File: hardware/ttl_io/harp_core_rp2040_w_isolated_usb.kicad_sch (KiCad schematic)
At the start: 49 parts, among them J1 Conn_01x03_Male, J2 AudioJack3, J3 USB_C_Receptacle_USB2.0, SW1 SW_Push, U1 TPD2EUSB30, U2 ADUM4160, U3 RP2040, U4 W25Q16JVUXIQ, X1 ECS-TXO-2016

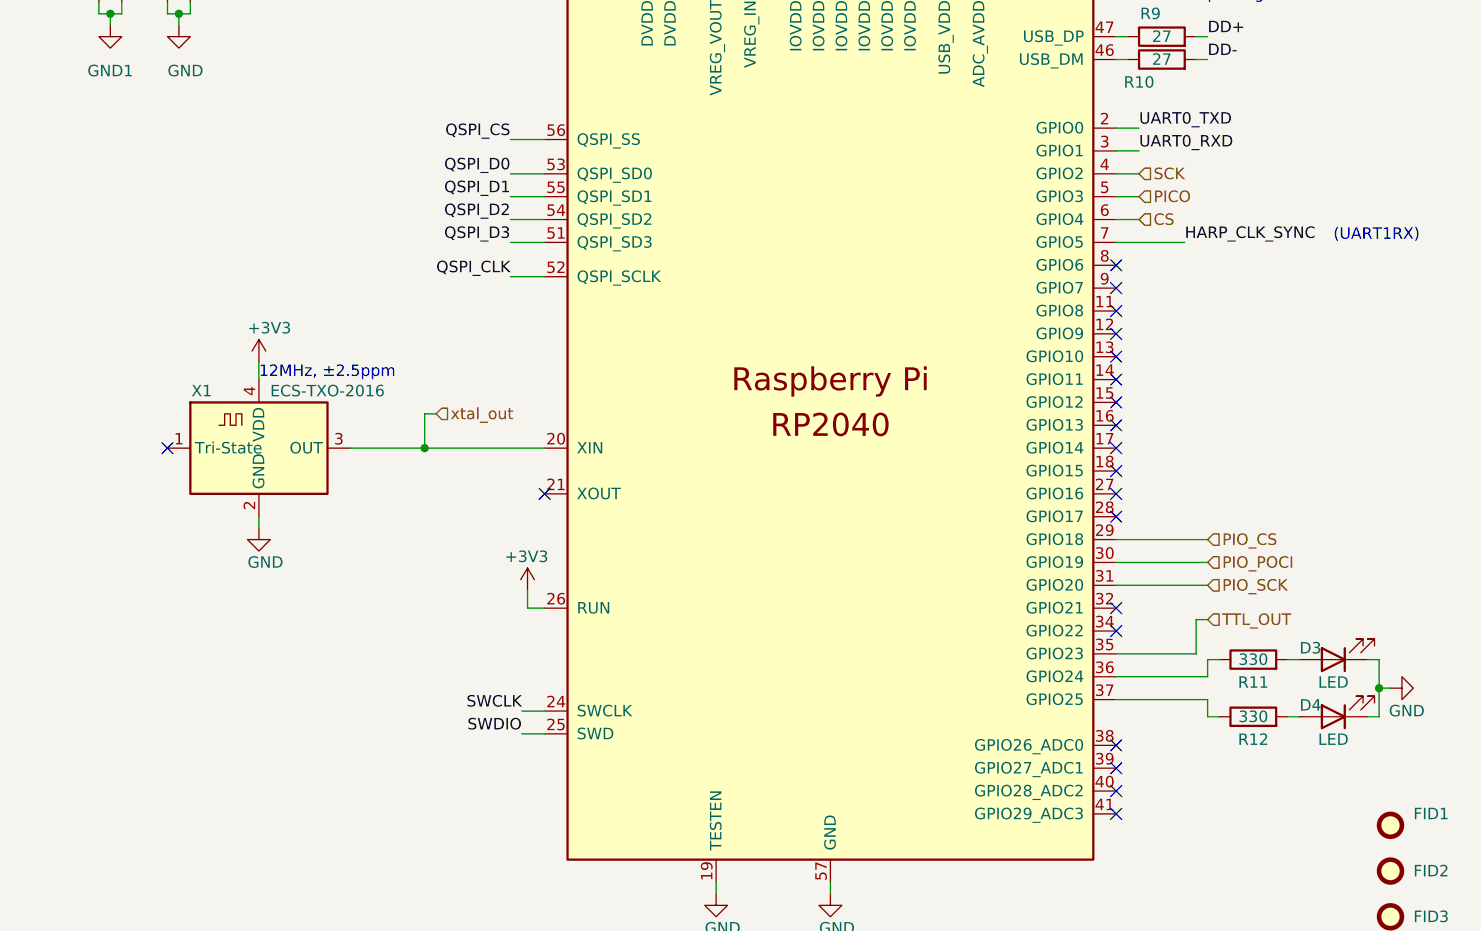
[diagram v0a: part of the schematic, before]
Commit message: draft mcu bypass with bus switches
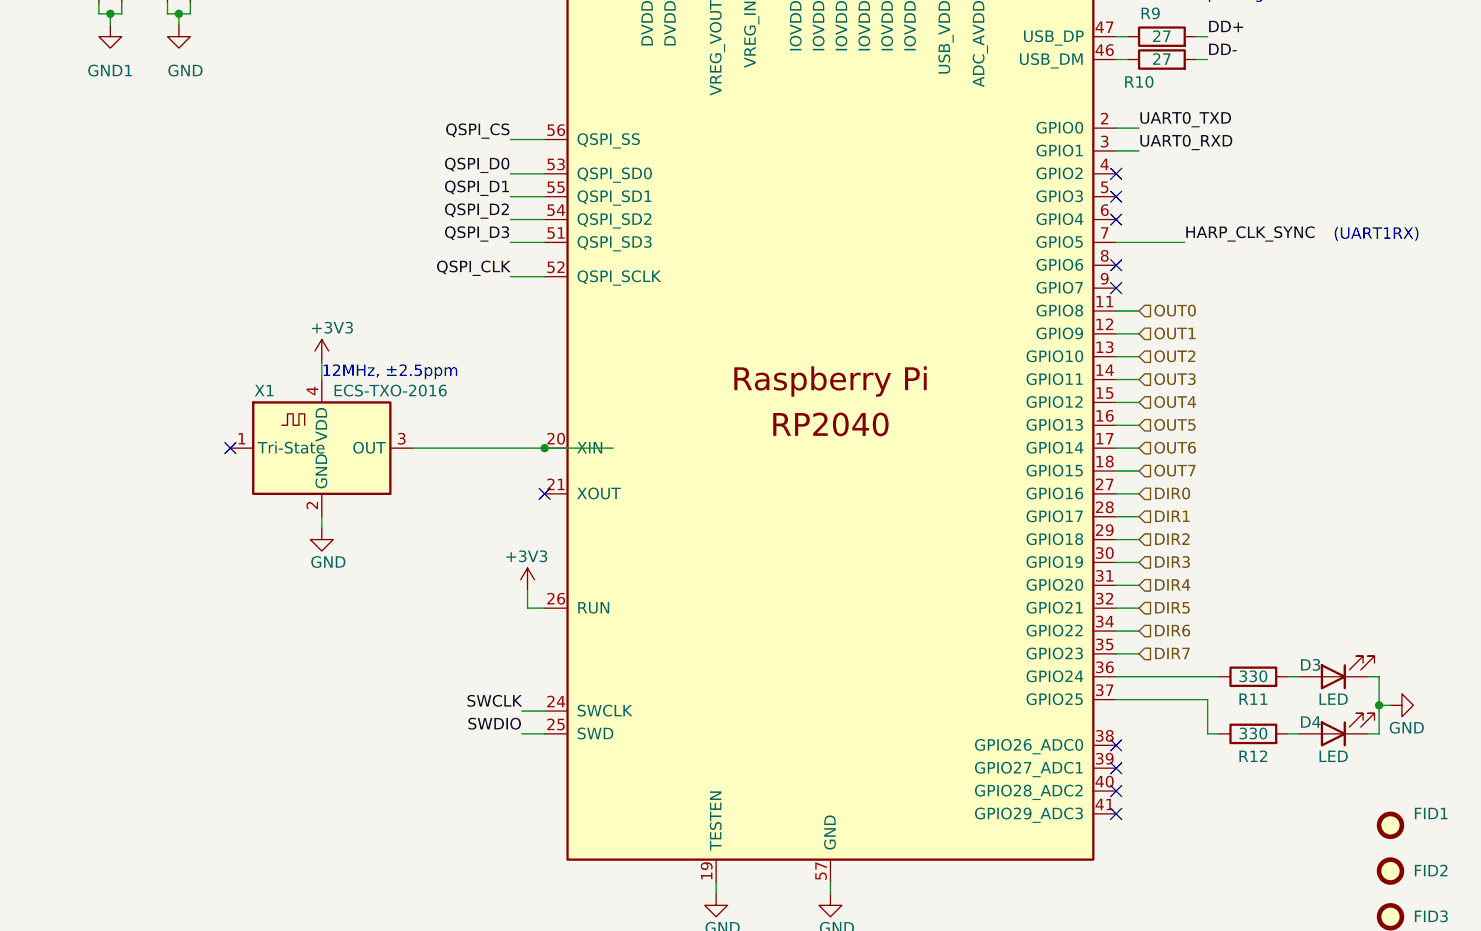
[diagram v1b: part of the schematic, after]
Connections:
- net OUT0: now reaches U3.11 (GPIO8)
- net OUT1: now reaches U3.12 (GPIO9)
- net OUT2: now reaches U3.13 (GPIO10)
- net OUT3: now reaches U3.14 (GPIO11)
- net OUT4: now reaches U3.15 (GPIO12)
- net OUT5: now reaches U3.16 (GPIO13)
- net OUT6: now reaches U3.17 (GPIO14)
- net OUT7: now reaches U3.18 (GPIO15)
- net DIR0: now reaches U3.27 (GPIO16)
- net DIR1: now reaches U3.28 (GPIO17)
- net DIR5: now reaches U3.32 (GPIO21)
- net DIR6: now reaches U3.34 (GPIO22)
- net CS: no longer names the net of U3.6 (GPIO4)
- net PICO: no longer names the net of U3.5 (GPIO3)
- net PIO_CS renamed DIR2
- net PIO_POCI renamed DIR3
- net PIO_SCK renamed DIR4
- net SCK: no longer names the net of U3.4 (GPIO2)
- net TTL_OUT renamed DIR7
- net xtal_out: no longer names the net of U3.20 (XIN), X1.3 (OUT)
- no-connect marks 22 -> 13
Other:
- moved on the sheet: D3, D4, R11, R12, X1

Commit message: update schematic with bus switches
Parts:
- D3, D4: footprint LED_SMD:LED_0603_1608Metric_Pad1.05x0.95mm_HandSolder -> LED_SMD:LED_0603_1608Metric
- R11, R12: value 330 -> 680; Link https://www.digikey.com/en/products/detail/panasonic-electr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 -> https://www.digikey.com/en/products/detail/yageo/RC0402FR-0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; Manufacturer Panasonic Electronic Components -> Yageo; Manufacturer Number ERA-2AEB331X -> RC0402FR-07680RL; Tolerance 0.1% -> 1%
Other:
- note added: "Green"
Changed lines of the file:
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@@
     (effects (font (size 1.27 1.27)) (justify left bottom))
   )
+  (text "Green" (at 265.43 130.81 0)
+    (effects (font (size 1.27 1.27)) (justify left bottom))
+  )
   (text "Close to package." (at 154.305 38.735 0)
     (effects (font (size 1.27 1.27)) (justify left bottom))
@@
     )
   )
-  (symbol (lib_id "Device:R") (at 259.715 141.605 90) (unit 1)
-    (in_bom yes) (on_board yes) (dnp no)
-    (property "Reference" "R12" (at 259.715 144.145 90)
-      (effects (font (size 1.27 1.27)))
-    )
-    (property "Value" "330" (at 259.715 141.605 90)
-      (effects (font (size 1.27 1.27)))
-    )
-    (property "Footprint" "Resistor_SMD:R_0402_1005Metric" (at 259.715 143.383 90)
-      (effects (font (size 1.27 1.27)) hide)
-    )
-    (property "Datasheet" "https://industrial.panasonic.com/cdbs/www-data/pdf/RDM0000/AOA0000C307.pdf" (at 259.715 141.605 0)
-      (effects (font (size 1.27 1.27)) hide)
-    )
-    (property "Link" "https://www.digikey.com/en/products/detail/panasonic-electronic-components/ERA-2AEB331X/1705993" (at 259.715 141.605 90)
-      (effects (font (size 1.27 1.27)) hide)
-    )
-    (property "Manufacturer" "Panasonic Electronic Components" (at 259.715 141.605 0)
-      (effects (font (size 1.27 1.27)) hide)
-    )
-    (property "Manufacturer Number" "ERA-2AEB331X" (at 259.715 141.605 0)
-      (effects (font (size 1.27 1.27)) hide)
-    )
-    (property "Tolerance" "0.1%" (at 259.715 141.605 0)
-      (effects (font (size 1.27 1.27)) hide)
-    )
-    (pin "1")
-    (pin "2")
-    (instances
-      (project "ttl_io"
-        (path "/de782c9d-fd54-45ed-aa91-6297331e40f6/1fe1f8ff-b1f9-48b6-8256-97b16d4120ca"
-          (reference "R12") (unit 1)
-        )
-      )
-      (project "harp_lick_detector_capactive"
-        (path "/e63e39d7-6ac0-4ffd-8aa3-1841a4541b55/eb8325ca-9747-4676-8e08-1fb825a7219f"
-          (reference "R13") (unit 1)
-        )
-      )
-    )
-  )
   (symbol (lib_id "Device:C") (at 47.625 149.225 180) (unit 1)
     (in_bom yes) (on_board yes) (dnp no)
@@
     )
   )
+  (symbol (lib_id "Device:R") (at 259.715 141.605 90) (unit 1)
+    (in_bom yes) (on_board yes) (dnp no)
+    (property "Reference" "R12" (at 259.715 144.145 90)
+      (effects (font (size 1.27 1.27)))
+    )
+    (property "Value" "680" (at 259.715 141.605 90)
+      (effects (font (size 1.27 1.27)))
+    )
+    (property "Footprint" "Resistor_SMD:R_0402_1005Metric" (at 259.715 143.383 90)
+      (effects (font (size 1.27 1.27)) hide)
+    )
+    (property "Datasheet" "https://www.yageo.com/upload/media/product/productsearch/datasheet/rchip/PYu-RC_Group_51_RoHS_L_12.pdf" (at 259.715 141.605 0)
+      (effects (font (size 1.27 1.27)) hide)
+    )
+    (property "Link" "https://www.digikey.com/en/products/detail/yageo/RC0402FR-07680RL/726654" (at 259.715 141.605 90)
+      (effects (font (size 1.27 1.27)) hide)
+    )
+    (property "Manufacturer" "Yageo" (at 259.715 141.605 0)
+      (effects (font (size 1.27 1.27)) hide)
+    )
+    (property "Manufacturer Number" "RC0402FR-07680RL" (at 259.715 141.605 0)
+      (effects (font (size 1.27 1.27)) hide)
+    )
+    (property "Tolerance" "1%" (at 259.715 141.605 0)
+      (effects (font (size 1.27 1.27)) hide)
+    )
+    (pin "1")
+    (pin "2")
+    (instances
+      (project "ttl_io"
+        (path "/de782c9d-fd54-45ed-aa91-6297331e40f6/1fe1f8ff-b1f9-48b6-8256-97b16d4120ca"
+          (reference "R12") (unit 1)
+        )
+      )
+      (project "harp_lick_detector_capactive"
+        (path "/e63e39d7-6ac0-4ffd-8aa3-1841a4541b55/eb8325ca-9747-4676-8e08-1fb825a7219f"
+          (reference "R12") (unit 1)
+        )
+      )
+    )
+  )
   (symbol (lib_id "Device:C") (at 160.655 184.785 180) (unit 1)
     (in_bom yes) (on_board yes) (dnp no)
@@
       (effects (font (size 1.27 1.27)))
     )
-    (property "Value" "330" (at 259.715 135.255 90)
+    (property "Value" "680" (at 259.715 135.255 90)
       (effects (font (size 1.27 1.27)))
     )
@@
       (effects (font (size 1.27 1.27)) hide)
     )
-    (property "Datasheet" "https://industrial.panasonic.com/cdbs/www-data/pdf/RDM0000/AOA0000C307.pdf" (at 259.715 135.255 0)
+    (property "Datasheet" "https://www.yageo.com/upload/media/product/productsearch/datasheet/rchip/PYu-RC_Group_51_RoHS_L_12.pdf" (at 259.715 135.255 0)
       (effects (font (size 1.27 1.27)) hide)
     )
-    (property "Link" "https://www.digikey.com/en/products/detail/panasonic-electronic-components/ERA-2AEB331X/1705993" (at 259.715 135.255 90)
+    (property "Link" "https://www.digikey.com/en/products/detail/yageo/RC0402FR-07680RL/726654" (at 259.715 135.255 90)
       (effects (font (size 1.27 1.27)) hide)
     )
-    (property "Manufacturer" "Panasonic Electronic Components" (at 259.715 135.255 0)
+    (property "Manufacturer" "Yageo" (at 259.715 135.255 0)
       (effects (font (size 1.27 1.27)) hide)
     )
-    (property "Manufacturer Number" "ERA-2AEB331X" (at 259.715 135.255 0)
+    (property "Manufacturer Number" "RC0402FR-07680RL" (at 259.715 135.255 0)
       (effects (font (size 1.27 1.27)) hide)
     )
-    (property "Tolerance" "0.1%" (at 259.715 135.255 0)
+    (property "Tolerance" "1%" (at 259.715 135.255 0)
       (effects (font (size 1.27 1.27)) hide)
     )
@@
       (effects (font (size 1.27 1.27)))
     )
-    (property "Footprint" "LED_SMD:LED_0603_1608Metric_Pad1.05x0.95mm_HandSolder" (at 268.605 141.605 0)
+    (property "Footprint" "LED_SMD:LED_0603_1608Metric" (at 268.605 141.605 0)
       (effects (font (size 1.27 1.27)) hide)
     )
@@
       (effects (font (size 1.27 1.27)))
     )
-    (property "Footprint" "LED_SMD:LED_0603_1608Metric_Pad1.05x0.95mm_HandSolder" (at 268.605 135.255 0)
+    (property "Footprint" "LED_SMD:LED_0603_1608Metric" (at 268.605 135.255 0)
       (effects (font (size 1.27 1.27)) hide)
     )

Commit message: update passthrough level translator
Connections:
- net SWCLK: no longer names the net of U3.24 (SWCLK)
- net SWDIO: no longer names the net of U3.25 (SWD)
- no-connect marks 13 -> 15
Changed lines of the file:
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@@
   (junction (at 151.765 179.705) (diameter 0) (color 0 0 0 0)
   )
+  (no_connect (at 180.975 139.065))
   (no_connect (at 244.475 92.075))
   (no_connect (at 146.05 109.855))
@@
   (no_connect (at 244.475 89.535))
   (no_connect (at 244.475 81.915))
+  (no_connect (at 180.975 141.605))
   (no_connect (at 180.975 114.935))
   (no_connect (at 244.475 79.375))
@@
     (stroke (width 0) (type default))
   )
-  (wire (pts (xy 17.78 142.24) (xy 17.78 144.78))
+  (wire (pts (xy 17.78 142.875) (xy 17.78 144.78))
     (stroke (width 0) (type default))
   )
@@
     (stroke (width 0) (type default))
   )
-  (wire (pts (xy 178.435 139.065) (xy 180.975 139.065))
-    (stroke (width 0) (type default))
-  )
   (wire (pts (xy 120.015 42.545) (xy 123.825 42.545))
     (stroke (width 0) (type default))
@@
     (stroke (width 0) (type default))
   )
-  (wire (pts (xy 178.435 141.605) (xy 180.975 141.605))
-    (stroke (width 0) (type default))
-  )
   (wire (pts (xy 38.735 140.335) (xy 38.735 145.415))
     (stroke (width 0) (type default))
@@
     (effects (font (size 1.27 1.27)) (justify right bottom))
   )
-  (label "SWDIO" (at 178.435 141.605 180) (fields_autoplaced)
-    (effects (font (size 1.27 1.27)) (justify right bottom))
-  )
   (label "UART0_RXD" (at 247.015 76.835 0) (fields_autoplaced)
     (effects (font (size 1.27 1.27)) (justify left bottom))
@@
     (effects (font (size 1.27 1.27)) (justify left bottom))
   )
-  (label "SWCLK" (at 178.435 139.065 180) (fields_autoplaced)
-    (effects (font (size 1.27 1.27)) (justify right bottom))
-  )
   (label "QSPI_CS" (at 241.935 33.655 180) (fields_autoplaced)
     (effects (font (size 1.27 1.27)) (justify right bottom))
@@
     )
   )
-  (symbol (lib_id "power:VBUS") (at 17.78 142.24 0) (unit 1)
+  (symbol (lib_id "power:VBUS") (at 17.78 142.875 0) (unit 1)
     (in_bom yes) (on_board yes) (dnp no)
-    (property "Reference" "#PWR03" (at 17.78 146.05 0)
+    (property "Reference" "#PWR03" (at 17.78 146.685 0)
       (effects (font (size 1.27 1.27)) hide)
     )
-    (property "Value" "VBUS" (at 17.78 138.43 0)
+    (property "Value" "VBUS" (at 17.78 139.065 0)
       (effects (font (size 1.27 1.27)))
     )
-    (property "Footprint" "" (at 17.78 142.24 0)
+    (property "Footprint" "" (at 17.78 142.875 0)
       (effects (font (size 1.27 1.27)) hide)
     )
-    (property "Datasheet" "" (at 17.78 142.24 0)
+    (property "Datasheet" "" (at 17.78 142.875 0)
       (effects (font (size 1.27 1.27)) hide)
     )

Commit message: annotate bus logic on schematic
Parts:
- R11, R12: value 680 -> 1K; Link https://www.digikey.com/en/products/detail/yageo/RC0402FR-0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 -> https://www.digikey.com/en/products/detail/yageo/RT0402BRD0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; Manufacturer Number RC0402FR-07680RL -> RT0402BRD071KL
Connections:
- net BUS_STATE: now reaches U3.4 (GPIO2)
- no-connect marks 15 -> 14
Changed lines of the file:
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@@
   (no_connect (at 180.975 141.605))
   (no_connect (at 180.975 114.935))
-  (no_connect (at 244.475 79.375))
   (no_connect (at 244.475 84.455))
   (no_connect (at 42.545 52.705))
@@
     (stroke (width 0) (type default))
   )
+  (wire (pts (xy 244.475 79.375) (xy 247.015 79.375))
+    (stroke (width 0) (type default))
+  )
   (wire (pts (xy 244.475 74.295) (xy 247.015 74.295))
     (stroke (width 0) (type default))
@@
     (effects (font (size 1.27 1.27)) (justify left))
   )
+  (hierarchical_label "BUS_STATE" (shape input) (at 247.015 79.375 0) (fields_autoplaced)
+    (effects (font (size 1.27 1.27)) (justify left))
+  )
   (hierarchical_label "DIR0" (shape input) (at 247.015 114.935 0) (fields_autoplaced)
     (effects (font (size 1.27 1.27)) (justify left))
@@
       (effects (font (size 1.27 1.27)))
     )
-    (property "Value" "680" (at 259.715 141.605 90)
+    (property "Value" "1K" (at 259.715 141.605 90)
       (effects (font (size 1.27 1.27)))
     )
@@
       (effects (font (size 1.27 1.27)) hide)
     )
-    (property "Datasheet" "https://www.yageo.com/upload/media/product/productsearch/datasheet/rchip/PYu-RC_Group_51_RoHS_L_12.pdf" (at 259.715 141.605 0)
+    (property "Datasheet" "n/a" (at 259.715 141.605 0)
       (effects (font (size 1.27 1.27)) hide)
     )
-    (property "Link" "https://www.digikey.com/en/products/detail/yageo/RC0402FR-07680RL/726654" (at 259.715 141.605 90)
+    (property "Link" "https://www.digikey.com/en/products/detail/yageo/RT0402BRD071KL/1069118" (at 259.715 141.605 90)
       (effects (font (size 1.27 1.27)) hide)
     )
@@
       (effects (font (size 1.27 1.27)) hide)
     )
-    (property "Manufacturer Number" "RC0402FR-07680RL" (at 259.715 141.605 0)
+    (property "Manufacturer Number" "RT0402BRD071KL" (at 259.715 141.605 0)
       (effects (font (size 1.27 1.27)) hide)
     )
@@
       (effects (font (size 1.27 1.27)))
     )
-    (property "Value" "680" (at 259.715 135.255 90)
+    (property "Value" "1K" (at 259.715 135.255 90)
       (effects (font (size 1.27 1.27)))
     )
@@
       (effects (font (size 1.27 1.27)) hide)
     )
-    (property "Datasheet" "https://www.yageo.com/upload/media/product/productsearch/datasheet/rchip/PYu-RC_Group_51_RoHS_L_12.pdf" (at 259.715 135.255 0)
+    (property "Datasheet" "n/a" (at 259.715 135.255 0)
       (effects (font (size 1.27 1.27)) hide)
     )
-    (property "Link" "https://www.digikey.com/en/products/detail/yageo/RC0402FR-07680RL/726654" (at 259.715 135.255 90)
+    (property "Link" "https://www.digikey.com/en/products/detail/yageo/RT0402BRD071KL/1069118" (at 259.715 135.255 90)
       (effects (font (size 1.27 1.27)) hide)
     )
@@
       (effects (font (size 1.27 1.27)) hide)
     )
-    (property "Manufacturer Number" "RC0402FR-07680RL" (at 259.715 135.255 0)
+    (property "Manufacturer Number" "RT0402BRD071KL" (at 259.715 135.255 0)
       (effects (font (size 1.27 1.27)) hide)
     )

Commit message: draft pcb v0.1.0
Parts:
- removed SW1: SW_Push, Button_Switch_SMD:SW_SPST_B3U-1000P, symbol Switch:SW_Push
- added SW1: ~, kicad_component_library:SW_Push_1P1T-SH_NO_Vertical_Wuerth_WS-TASV, symbol kicad_component_library:SW_Push_with_gnd
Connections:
- net GND: now also SW1.4, SW1.SH
- net USB_Boot: now also SW1.2
- no-connect marks 14 -> 16
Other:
- note added: "C10 must be near VREG_OUT."
- note added: "C12 must be near VREG_IN."
- note removed: "C10 must be near VREG_IN."
- note removed: "C9 must be near VREG_OUT."
- moved on the sheet: R1
